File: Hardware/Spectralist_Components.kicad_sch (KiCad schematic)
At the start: 94 parts, among them J1 Conn_01x12_Pin, J2 Conn_01x12_Pin, J3 Conn_01x10_Pin, J4 Conn_01x10_Pin, J5 Eurorack_10_pin_power, J6 SWD_Header, J7 Conn_01x02_Pin, U2 PCM5100APW, U3 TPS561201, U4 LT1117-3.3, U5 MCP6002, U6 STM32H723VGTx, U7 MCP6004, U8 TL072, Y1 8MHz 20pF

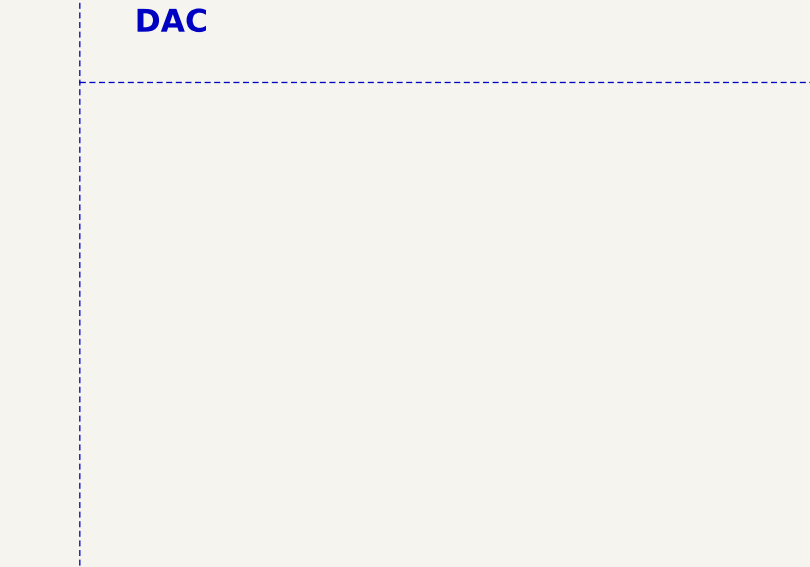
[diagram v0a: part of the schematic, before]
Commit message: Curvy traces on LED board
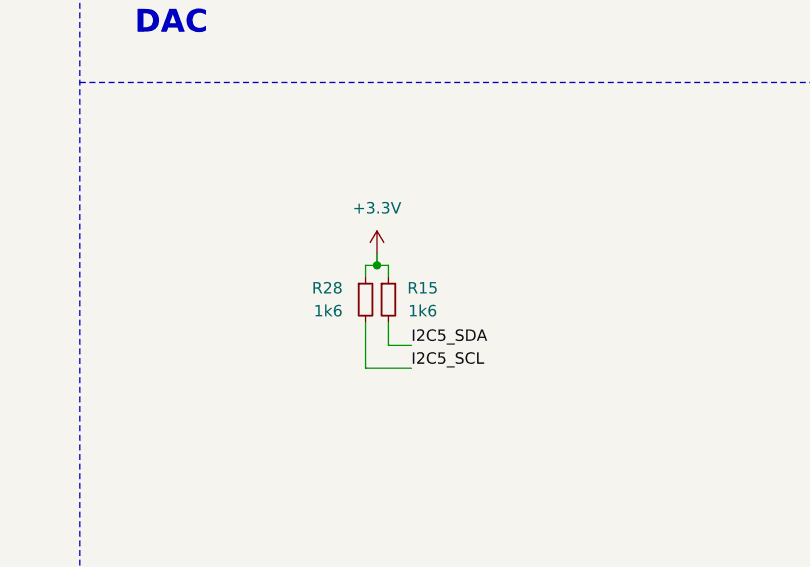
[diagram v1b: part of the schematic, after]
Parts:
- added R15, R28: 1k6, Resistor_SMD:R_0603_1608Metric, symbol Device:R_Small
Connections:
- net +3.3V: now also R15.1, R28.1
- net I2C5_SCL: now also R28.2
- net I2C5_SDA: now also R15.2

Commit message: Component PCB updates
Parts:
- removed C37: 2.2nF, Capacitor_SMD:C_0603_1608Metric, symbol Device:C_Small
- removed J1, J2: Conn_01x12_Pin, Connector_PinHeader_2.54mm:PinHeader_1x12_P2.54mm_Vertical, symbol Connector:Conn_01x12_Pin
- removed R31: 100k, Resistor_SMD:R_0603_1608Metric, symbol Device:R_Small
- removed R34: 6k8, Resistor_SMD:R_0603_1608Metric, symbol Device:R
- removed U5: MCP6002, Package_SO:SOIC-8_3.9x4.9mm_P1.27mm, symbol Amplifier_Operational:MCP6002-xSN
- added J1, J2: Conn_01x10_Pin, Connector_PinHeader_2.54mm:PinHeader_1x10_P2.54mm_Vertical, symbol Connector:Conn_01x10_Pin
- added R29, R31: 75k, Resistor_SMD:R_0603_1608Metric, symbol Device:R
- added R34, R37: 10k, Resistor_SMD:R_0603_1608Metric, symbol Device:R_Small
- added R35: 82k, Resistor_SMD:R_0603_1608Metric, symbol Device:R
- added R36: 47k, Resistor_SMD:R_0603_1608Metric, symbol Device:R
- added R38, R39: 1k, Resistor_SMD:R_0603_1608Metric, symbol Device:R_Small
- added U5: MCP6004, Package_SO:SO-14_3.9x8.65mm_P1.27mm, symbol Amplifier_Operational:MCP6004
- R32: value 20k -> 82k; Part_Number C4184 -> C23265
- R33: value 33k -> 47k
- renumbered U6 to U1
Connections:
- net AudioIn is gone; now on net Filter_A_CV: U7.1
- net LED_Oct_B is gone; now on net LED_Oct: R30.1
- net VCA_CV_In is gone; now on net Harm_Stretch_CV_In: R26.2
- net V_Oct_CV is gone; now on net Filter_Slope_Pot: U1.33 (PC5)
- net VcaCV is gone; now on net Harm_Stretch_CV: R27.1, U7.14
- net WarpCV is gone; now on net Filter_B_CV: R13.1, U7.7
- net Warp_CV_In is gone; now on net Filter_B_CV_In: R20.2
- net WavetablePosA_CV is gone; now on net Harm_Warp_CV: R19.1
- net WavetablePosB_CV is gone; now on net Filter_Slope_CV: R21.1, U7.8
- net Wavetable_Pos_A_CV_In is gone; now on net Harm_Warp_CV_In: R17.2
- net Wavetable_Pos_B_CV_In is gone; now on net Filter_Slope_CV_In: R12.2
- net +12V: now also J2.2 (Pin_2)
- net +3.3V: now also U1.100 (VDD), J2.1 (Pin_1), R34.2
- net +3.3VA: now also U1.21 (VDDA), U5.4 (V+); no longer U1.100 (VDD)
- net -5V_REF: now also R29.2, R31.2; no longer R32.2
- net Audio_Out_L: now also J3.7 (Pin_7)
- net Audio_Out_R: now also J3.8 (Pin_8)
- net Filter_A_CV: now also U1.24 (PA2), R36.1; no longer U1.23 (PA1)
- net Filter_A_Pot: now also U1.23 (PA1), J2.8 (Pin_8); no longer U1.22 (PA0)
- net Filter_A_Trm: now also U1.22 (PA0), J2.7 (Pin_7); no longer U1.24 (PA2)
- net Filter_B_CV: now also U1.25 (PA3); no longer U1.28 (PA4)
- net Filter_B_Pot: now also J3.2 (Pin_2), U1.31 (PA7); no longer U1.25 (PA3)
- net Filter_B_Trm: now also J3.3 (Pin_3), U1.32 (PC4); no longer U1.29 (PA5)
- net Filter_Mode: now also J2.3 (Pin_3)
- net Filter_Slope_Pot: now also J3.1 (Pin_1); no longer U1.30 (PA6)
- net GND: now also U1.10 (VSS), U1.19 (VSSA), U1.26 (VSS), U1.49 (VSS), U1.74 (VSS), U1.99 (VSS), J1.1 (Pin_1), J1.4 (Pin_4), J2.5 (Pin_5), R37.1, U5.10 (+), U5.11 (V-), U5.3 (+), U5.5 (+)
- net Harm_Stretch_CV: now also U1.29 (PA5); no longer U1.35 (PB1)
- net Harm_Stretch_Pot: now also J3.5 (Pin_5), U1.35 (PB1); no longer U1.31 (PA7)
- net Harm_Stretch_Trm: now also J3.4 (Pin_4)
- net Harm_Warp_CV: now also U5.7
- net Harm_Warp_Pot: now also J3.6 (Pin_6)
- net I2C5_SCL: now also J1.2 (Pin_2)
- net I2C5_SDA: now also J1.3 (Pin_3)
- net Octave_Btn: now also U1.3 (PE4), J2.6 (Pin_6); no longer U1.57 (PD10)
- net Pan_CV: now also R33.1, U1.30 (PA6), U5.8; no longer U1.32 (PC4)
- net Pitch_CV_In: now also J4.6 (Pin_6)
- net Pitch_CV_Scaled: now also U1.28 (PA4), U5.1
- net Warp_Mode: now also J2.4 (Pin_4)
- net at C35.2, R22.1, R23.1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: now also U5.2 (-)
- net at R16.1, R17.1, R19.2: now also U5.6 (-)
- net LED_Filter_B: now reaches U1.60 (PD13)
- net LED_Filter_B: now also R39.1
- net LED_Filter_A: now reaches U1.62 (PD15)
- net LED_Filter_A: now also R38.1
- net Harm_Stretch_CV_In: now reaches J4.2 (Pin_2)
- net Filter_A_CV_In: now reaches J4.3 (Pin_3)
- net Filter_A_CV_In: now also R35.2
- net Filter_B_CV_In: now reaches J4.4 (Pin_4)
- net Filter_Slope_CV_In: now reaches J4.5 (Pin_5)
- net Harm_Warp_CV_In: now reaches J4.8 (Pin_8)
- net Pan_CV_In: now reaches J4.9 (Pin_9)
- net Pan_CV_In: now also R32.2
- net Ext_Audio_In: no longer names the net of R33.2
- net Ext_Audio_In: now also R32.1, R31.1, U5.9 (-)
- net LED_Oct_B_Out renamed LED_Oct_Out
- net LED_Oct_Out: now also J1.6 (Pin_6)
- new net: R29.1, R35.1, R36.2, U7.2 (-)
- new net: R34.1, R37.2, U5.12 (+)
- new net: U5.13 (-), U5.14
- new net LED_Filter_A_Out: J1.5 (Pin_5), R38.2
- new net LED_Filter_B_Out: J1.7 (Pin_7), R39.2
- no-connect marks 30 -> 48
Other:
- note removed: "(-5*-6.8/20) + (cv*-6.8/33): -8V > 3.35V; +8V > 0.05V"
- note removed: "22ohms gives 150mA"
- moved on the sheet: C16, C17, C18, C19, C20, C21, C22, C23, C24, R15, R28

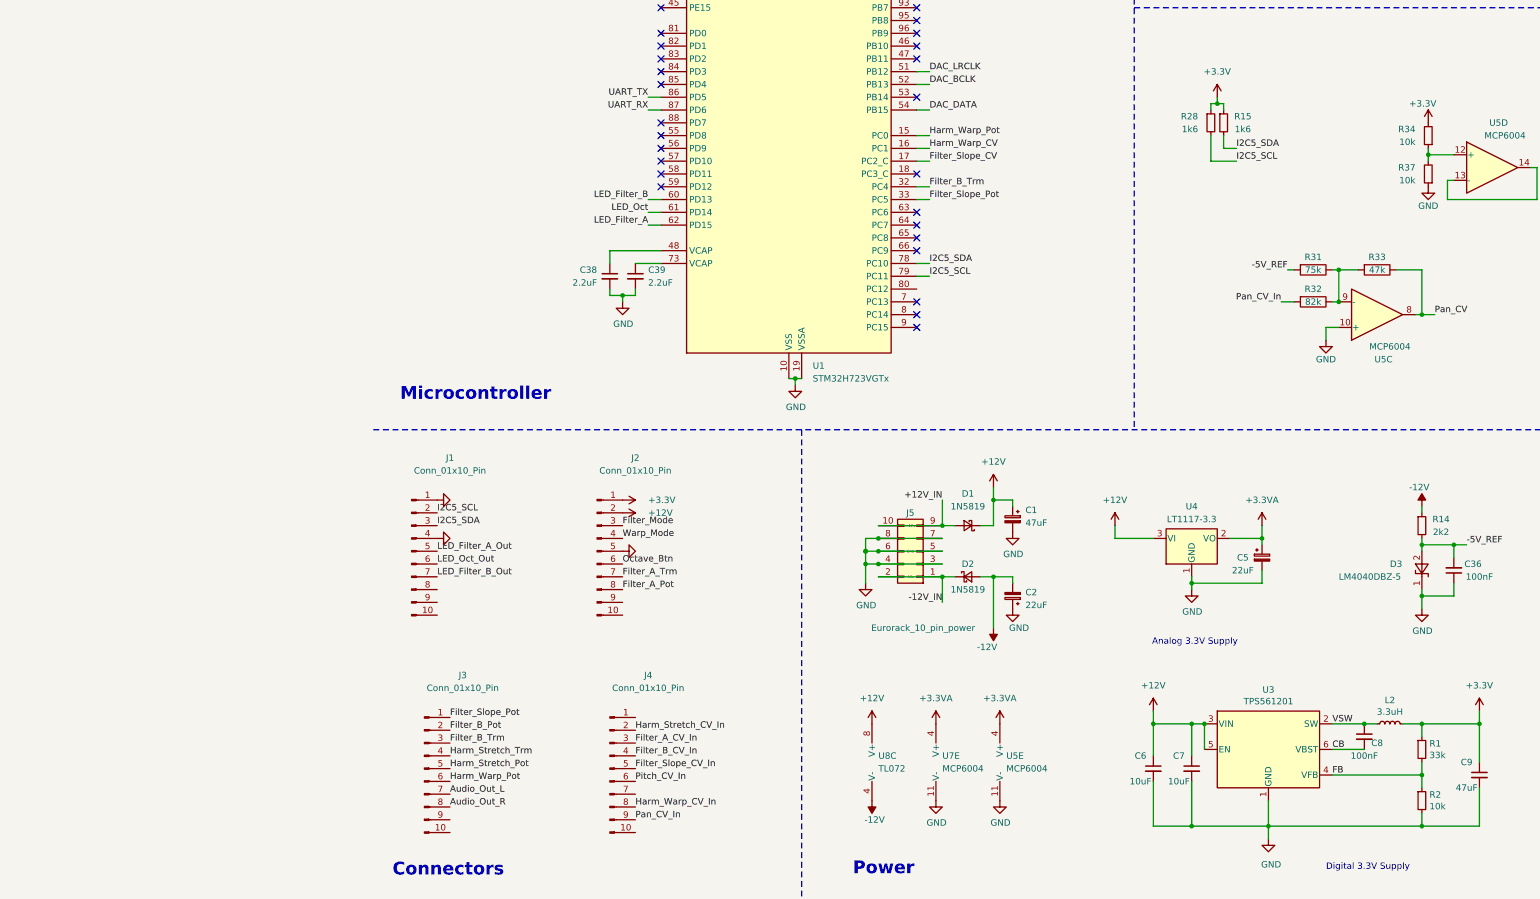
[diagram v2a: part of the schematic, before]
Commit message: Started adding USB
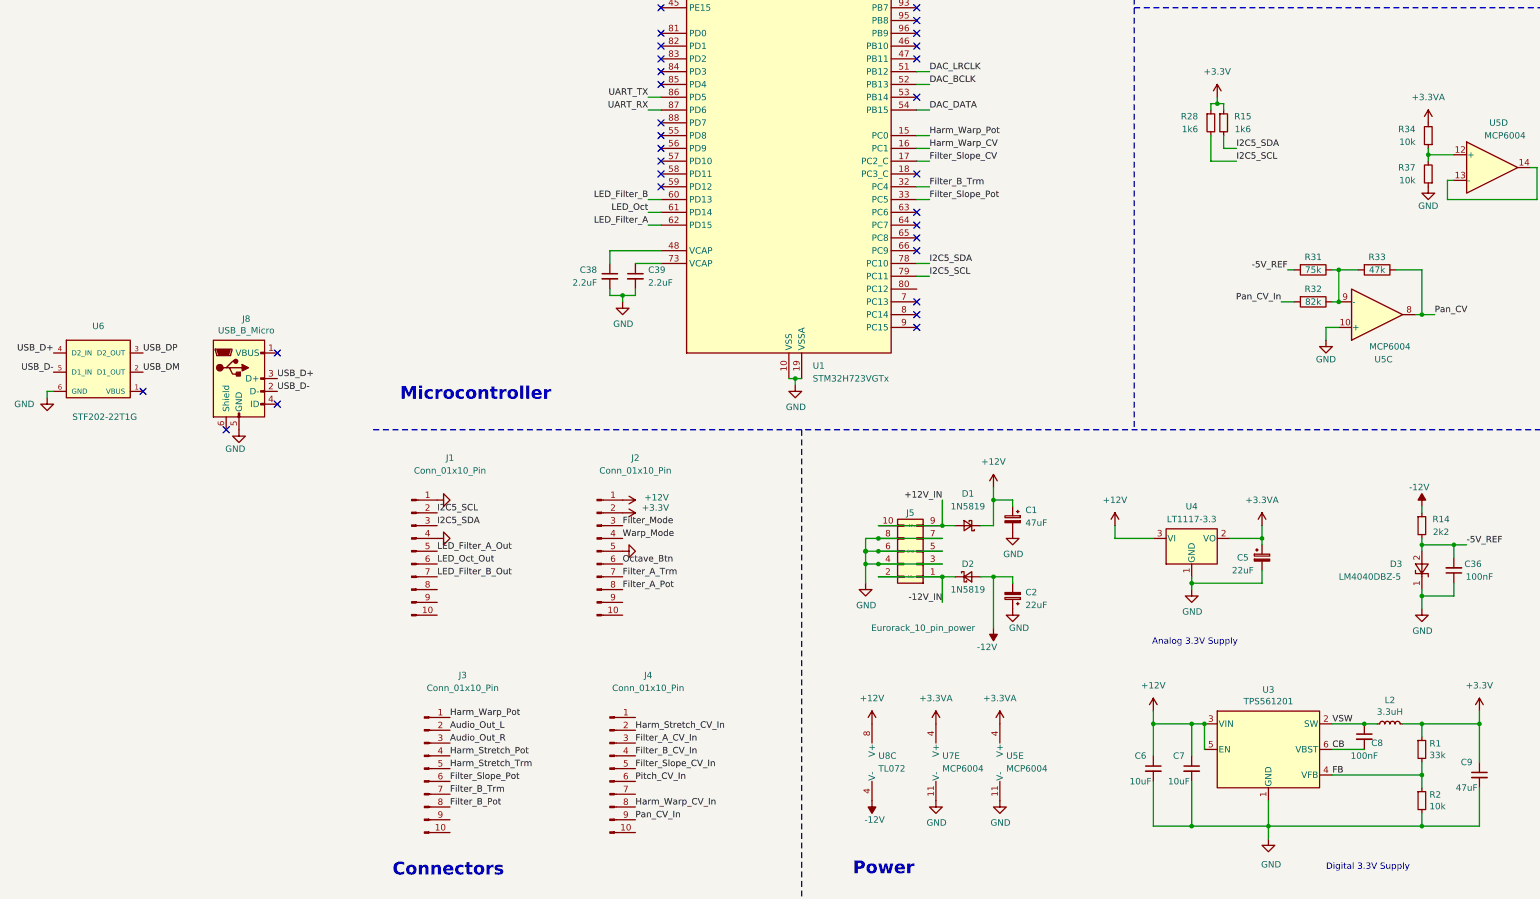
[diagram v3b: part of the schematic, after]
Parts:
- added J8: USB_B_Micro, Custom_Footprints:USB_Micro-B_Amphenol, symbol Connector:USB_B_Micro
- added U6: STF202-22T1G, Custom_Footprints:STF202-22T1G, symbol STF202-22T1G:STF202-22T1G
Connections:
- net +12V: now also J2.1 (Pin_1); no longer J2.2 (Pin_2)
- net +3.3V: now also J2.2 (Pin_2); no longer J2.1 (Pin_1), R34.2
- net +3.3VA: now also R34.2
- net Audio_Out_L: now also J3.2 (Pin_2); no longer J3.7 (Pin_7)
- net Audio_Out_R: now also J3.3 (Pin_3); no longer J3.8 (Pin_8)
- net Filter_B_Pot: now also J3.8 (Pin_8); no longer J3.2 (Pin_2)
- net Filter_B_Trm: now also J3.7 (Pin_7); no longer J3.3 (Pin_3)
- net Filter_Slope_Pot: now also J3.6 (Pin_6); no longer J3.1 (Pin_1)
- net GND: now also J8.5 (GND), U6.6 (GND)
- net Harm_Stretch_Pot: now also J3.4 (Pin_4); no longer J3.5 (Pin_5)
- net Harm_Stretch_Trm: now also J3.5 (Pin_5); no longer J3.4 (Pin_4)
- net Harm_Warp_Pot: now also J3.1 (Pin_1); no longer J3.6 (Pin_6)
- net USB_DM: now also U6.2 (D1_OUT)
- net USB_DP: now also U6.3 (D2_OUT)
- new net USB_D+: J8.3 (D+), U6.4 (D2_IN)
- new net USB_D-: J8.2 (D-), U6.5 (D1_IN)
- no-connect marks 48 -> 52

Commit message: More layout on Component and Control boards
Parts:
- J1, J2: value Conn_01x10_Pin -> Conn_01x08_Pin; footprint Connector_PinHeader_2.54mm:PinHeader_1x10_P2.54mm_Vertical -> Connector_PinHeader_2.54mm:PinHeader_1x08_P2.54mm_Vertical; symbol Connector:Conn_01x10_Pin -> Connector:Conn_01x08_Pin
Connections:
- net +12V: now also J2.8 (Pin_8); no longer J2.1 (Pin_1)
- net +3.3V: now also J2.1 (Pin_1); no longer J2.2 (Pin_2)
- net Audio_Out_R: now also J3.4 (Pin_4); no longer J3.3 (Pin_3)
- net Filter_A_CV: now also R33.1, U1.30 (PA6), U5.8; no longer R36.1, U1.24 (PA2), U7.1
- net Filter_A_CV_In: now also J4.10 (Pin_10), R32.2; no longer J4.3 (Pin_3), R35.2
- net Filter_A_Pot: now also J2.6 (Pin_6), U1.22 (PA0); no longer J2.8 (Pin_8), U1.23 (PA1)
- net Filter_A_Trm: now also U1.23 (PA1); no longer U1.22 (PA0)
- net Filter_B_CV: now also R36.1, U1.24 (PA2), U7.1; no longer R13.1, U1.25 (PA3), U7.7
- net Filter_B_CV_In: now also J4.3 (Pin_3), R35.2; no longer J4.4 (Pin_4), R20.2
- net Filter_B_Pot: now also J3.6 (Pin_6), U1.34 (PB0); no longer J3.8 (Pin_8), U1.31 (PA7)
- net Filter_B_Trm: now also J3.1 (Pin_1), U1.15 (PC0); no longer J3.7 (Pin_7), U1.32 (PC4)
- net Filter_Mode: now also J2.2 (Pin_2); no longer J2.3 (Pin_3)
- net Filter_Slope_CV: now also R13.1, U1.25 (PA3), U7.7; no longer R21.1, U1.17 (PC2_C), U7.8
- net Filter_Slope_CV_In: now also R20.2; no longer R12.2
- net Filter_Slope_Pot: now also J3.5 (Pin_5), U1.35 (PB1); no longer J3.6 (Pin_6), U1.33 (PC5)
- net GND: now also J1.7 (Pin_7), J2.4 (Pin_4), J3.3 (Pin_3), J3.7 (Pin_7), J4.1 (Pin_1), J4.4 (Pin_4), J4.7 (Pin_7); no longer J2.5 (Pin_5)
- net Harm_Stretch_CV: now also R19.1, U1.16 (PC1), U5.7; no longer R27.1, U1.29 (PA5), U7.14
- net Harm_Stretch_CV_In: now also J4.9 (Pin_9), R17.2; no longer J4.2 (Pin_2), R26.2
- net Harm_Stretch_Pot: now also J3.9 (Pin_9), U1.32 (PC4); no longer J3.4 (Pin_4), U1.35 (PB1)
- net Harm_Stretch_Trm: now also J3.8 (Pin_8), U1.33 (PC5); no longer J3.5 (Pin_5), U1.34 (PB0)
- net Harm_Warp_CV: now also R27.1, U1.29 (PA5), U7.14; no longer R19.1, U1.16 (PC1), U5.7
- net Harm_Warp_CV_In: now also J4.2 (Pin_2), R26.2; no longer J4.8 (Pin_8), R17.2
- net Harm_Warp_Pot: now also J3.10 (Pin_10), U1.31 (PA7); no longer J3.1 (Pin_1), U1.15 (PC0)
- net LED_Filter_B_Out: now also J1.8 (Pin_8); no longer J1.7 (Pin_7)
- net Octave_Btn: now also J2.5 (Pin_5); no longer J2.6 (Pin_6)
- net Pan_CV: now also R21.1, U1.17 (PC2_C), U7.8; no longer R33.1, U1.30 (PA6), U5.8
- net Pan_CV_In: now also J4.6 (Pin_6), R12.2; no longer J4.9 (Pin_9), R32.2
- net Pitch_CV_In: now also J4.8 (Pin_8); no longer J4.6 (Pin_6)
- net USB_VBUS: now also J8.1 (VBUS)
- net I2C5_SCL renamed LED_SCL
- net I2C5_SDA renamed LED_SDA
- net Warp_Mode renamed Harmonic_Mode
- net Harmonic_Mode: now also J2.3 (Pin_3); no longer J2.4 (Pin_4)
- no-connect marks 52 -> 51
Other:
- note added: "LEDs on I2C5"
- moved on the sheet: R31, R32, R33, U5C

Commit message: More PCB Layout
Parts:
- J7: value Conn_01x02_Pin -> UART_Test_Pins
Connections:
- net Filter_B_Pot: now also J3.1 (Pin_1), U1.15 (PC0); no longer J3.6 (Pin_6), U1.34 (PB0)
- net Filter_B_Trm: now also J3.6 (Pin_6), U1.34 (PB0); no longer J3.1 (Pin_1), U1.15 (PC0)
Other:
- note added: "USB/Connectors"
- moved on the sheet: C29, C30, C31, C32, C35, J1, J2, J3, J4, J6, J7, J8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

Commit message: Started adding JLC part numbers
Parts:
- R10, R9: value 1k -> 100
- R12, R17, R20, R23, R26, R32, R35: value 82k -> 100k
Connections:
- net +3.3VA: now also J4.1 (Pin_1)
- net Filter_A_CV: now also R21.1, U1.17 (PC2_C), U7.8; no longer R33.1, U1.30 (PA6), U5.8
- net Filter_A_CV_In: now also J4.7 (Pin_7), R12.2; no longer J4.10 (Pin_10), R32.2
- net Filter_B_CV: now also R33.1, U1.30 (PA6), U5.8; no longer R36.1, U1.24 (PA2), U7.1
- net Filter_B_CV_In: now also J4.10 (Pin_10), R32.2; no longer J4.3 (Pin_3), R35.2
- net Filter_B_Pot: now also J3.5 (Pin_5), U1.35 (PB1); no longer J3.1 (Pin_1), U1.15 (PC0)
- net Filter_B_Trm: now also J3.1 (Pin_1), U1.15 (PC0); no longer J3.6 (Pin_6), U1.34 (PB0)
- net Filter_Slope_Pot: now also J3.6 (Pin_6), U1.34 (PB0); no longer J3.5 (Pin_5), U1.35 (PB1)
- net GND: now also J4.2 (Pin_2), J4.6 (Pin_6); no longer J4.1 (Pin_1), J4.4 (Pin_4), J4.7 (Pin_7)
- net Harm_Stretch_CV: now also R27.1, U1.29 (PA5), U7.14; no longer R19.1, U1.16 (PC1), U5.7
- net Harm_Stretch_CV_In: now also J4.3 (Pin_3), R26.2; no longer J4.9 (Pin_9), R17.2
- net Harm_Stretch_Pot: now also J3.10 (Pin_10), U1.31 (PA7); no longer J3.9 (Pin_9), U1.32 (PC4)
- net Harm_Stretch_Trm: now also J3.9 (Pin_9), U1.32 (PC4); no longer J3.8 (Pin_8), U1.33 (PC5)
- net Harm_Warp_CV: now also R24.1, U1.28 (PA4), U5.1; no longer R27.1, U1.29 (PA5), U7.14
- net Harm_Warp_CV_In: now also J4.8 (Pin_8), R23.2; no longer J4.2 (Pin_2), R26.2
- net Harm_Warp_Pot: now also J3.8 (Pin_8), U1.33 (PC5); no longer J3.10 (Pin_10), U1.31 (PA7)
- net Pan_CV: now also R19.1, U1.16 (PC1), U5.7; no longer R21.1, U1.17 (PC2_C), U7.8
- net Pan_CV_In: now also J4.9 (Pin_9), R17.2; no longer J4.6 (Pin_6), R12.2
- net Pitch_CV_In: now also J4.4 (Pin_4), R35.2; no longer J4.8 (Pin_8), R23.2
- net Pitch_CV_Scaled: now also R36.1, U1.24 (PA2), U7.1; no longer R24.1, U1.28 (PA4), U5.1
- net at R22.1, R23.1, R24.2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: no longer C35.2
- net at R29.1, R35.1, R36.2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: now also C35.2
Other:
- note added: "(-5*-47/75) + (cv*-47/100): 0V > 3.13V; 6.67V > 0V"
- note removed: "(-5*-47/75) + (cv*-47/82): 0V > 3.13V; 5.46V > 0V"
- note removed: "Bipolar: (-5*-47/150) + (cv*-47/150): -5V > 3.13V; 0V > 1.57V; 5V > 0V"
- moved on the sheet: C35, J3, R22, R23, R24, R29, R31, R32, R33, R35, R36, U5A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

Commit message: v1.0 PCBs sent to production
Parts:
- J7: footprint Connector_PinHeader_2.54mm:PinHeader_1x02_P2.54mm_Vertical -> Connector_PinHeader_2.54mm:PinHeader_1x03_P2.54mm_Vertical; symbol Connector:Conn_01x02_Pin -> Connector:Conn_01x03_Pin
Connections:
- net UART_RX: now also J7.3 (Pin_3); no longer J7.2 (Pin_2)
- net UART_TX: now also J7.2 (Pin_2); no longer J7.1 (Pin_1)
- net SPI3_NSS: now reaches U1.77 (PA15(JTDI))
- net SPI3_NSS: now also J7.1 (Pin_1)
- no-connect marks 51 -> 50
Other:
- moved on the sheet: R15, R28

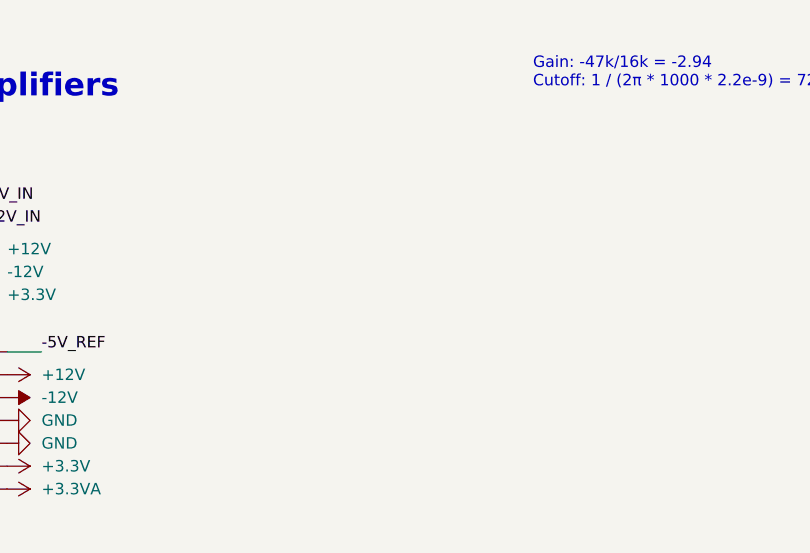
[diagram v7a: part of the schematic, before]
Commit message: Started bring up of v1 production board
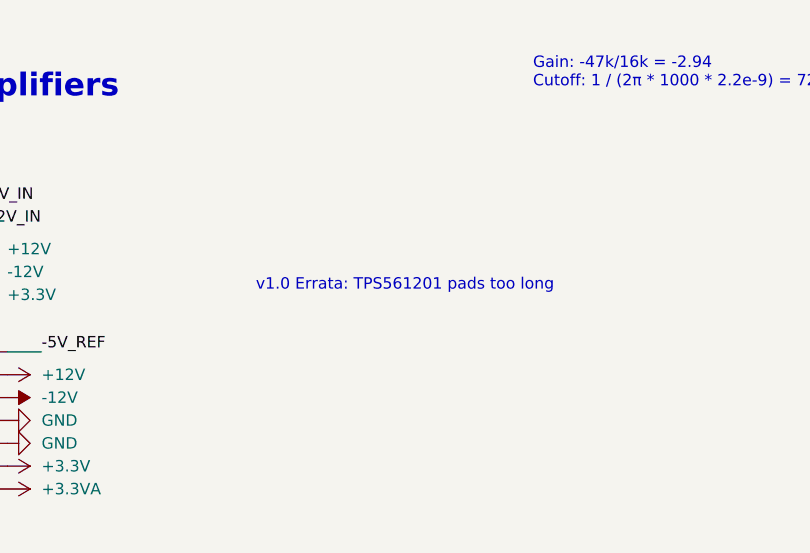
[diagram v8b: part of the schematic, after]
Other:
- note added: "v1.0 Errata: TPS561201 pads too long"
